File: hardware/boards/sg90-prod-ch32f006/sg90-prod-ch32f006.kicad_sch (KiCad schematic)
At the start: 21 parts, among them J1 Servo Input, J2 Debug, J3 Motor, J4 Potentiometer, Q1 BRCS150P02ZJ, U1 CH32V006F8U6, U2 DRV8837C, U3 74LVC1G07

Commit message: re-organize shared folders
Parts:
- removed C7: 10µF, Capacitor_SMD:C_0603_1608Metric, symbol Device:C
- added D1: PESD5V0L1UL, Diode_SMD:D_SOD-882, symbol Diode:PESD5V0L1UL
- added NT1, NT2, NT3, NT4: NetTie_2, shared:NetTie-2_SMD_0.2mm, symbol Device:NetTie_2
- J1: footprint common:Servo_Output_Pads -> shared:Servo_Output_Pads
- J2: footprint common:Debug_Pads_1x4_P1.27mm -> shared:Debug_Pads_1x4_P1.27mm
- J3: footprint common:Motor_Wire_Pads -> shared:Motor_Wire_Pads
- J4: footprint common:Pot_Wire_Pads -> shared:Pot_Wire_Pads
- Q1: footprint footprints:DFN-6L_L2.0-W2.0-P0.65-BL_BRCS300PXX -> shared:DFN-6L_L2.0-W2.0-P0.65-BL_BRCS300PXX; symbol common:BRCS150P02ZJ -> shared:BRCS150P02ZJ
- U1: renamed from U3; footprint footprints:TDFN-6_L1.0-W1.0-P0.35-BL -> shared:TDFN-6_L1.0-W1.0-P0.35-BL; symbol common:SN74LVC1G07DSFR_C42445855 -> shared:SN74LVC1G07DSFR_C42445855
- U3: renamed from U1; footprint common:UQFN-20_L3.0-W3.0-P0.40-BL-EP1.7 -> shared:UQFN-20_L3.0-W3.0-P0.40-BL-EP1.7; symbol common:CH32V006F8U6 -> shared:CH32V006F8U6
- renumbered C6 to C1, C1 to C2, C4 to C3, C3 to C4, C2 to C6, R4 to R1, R9 to R2, R2 to R4, R1 to R7
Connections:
- net V_MCU is gone; now on net +5V: J4.3 (Pin_3)
- net DATA: now also D1.1 (K), NT1.1; no longer U3.8 (PC1)
- net GND: now also R4.1, D1.2 (A); no longer R4.2
- net GND_MOT: now also R4.2, NT2.2; no longer R4.1, U3.2 (PA1/OPN0), U3.3 (PA2/OPP0)
- net MOT_A: now also J3.1 (Pin_1), NT3.2; no longer J3.2 (Pin_2), U3.16 (PD2)
- net MOT_B: now also J3.2 (Pin_2), NT4.2; no longer J3.1 (Pin_1), U3.17 (PD3)
- new net SEN_A: NT3.1, U3.16 (PD2/T1/T2/U2TX_/A3)
- new net SEN_B: NT4.1, U3.17 (PD3/T1/T2/U2RX_/NSS_/OPP2/A4)
- new net SEN_I: NT2.1, U3.2 (PA1/T1/T2/OPN0/XI/A1), U3.3 (PA2/T1/T2/U2TX_/OPP0/XO/A0)
- new net UART_RX: NT1.2, U3.8 (PC1/T1C2N_/T2/RX_/SDA/NSS)
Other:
- note added: "KELVIN TRACES"
- note added: "POTENTIOMETER"
- moved on the sheet: C3, C4, C5, C6, J1, R3, R4, R5, R7, U2, U3

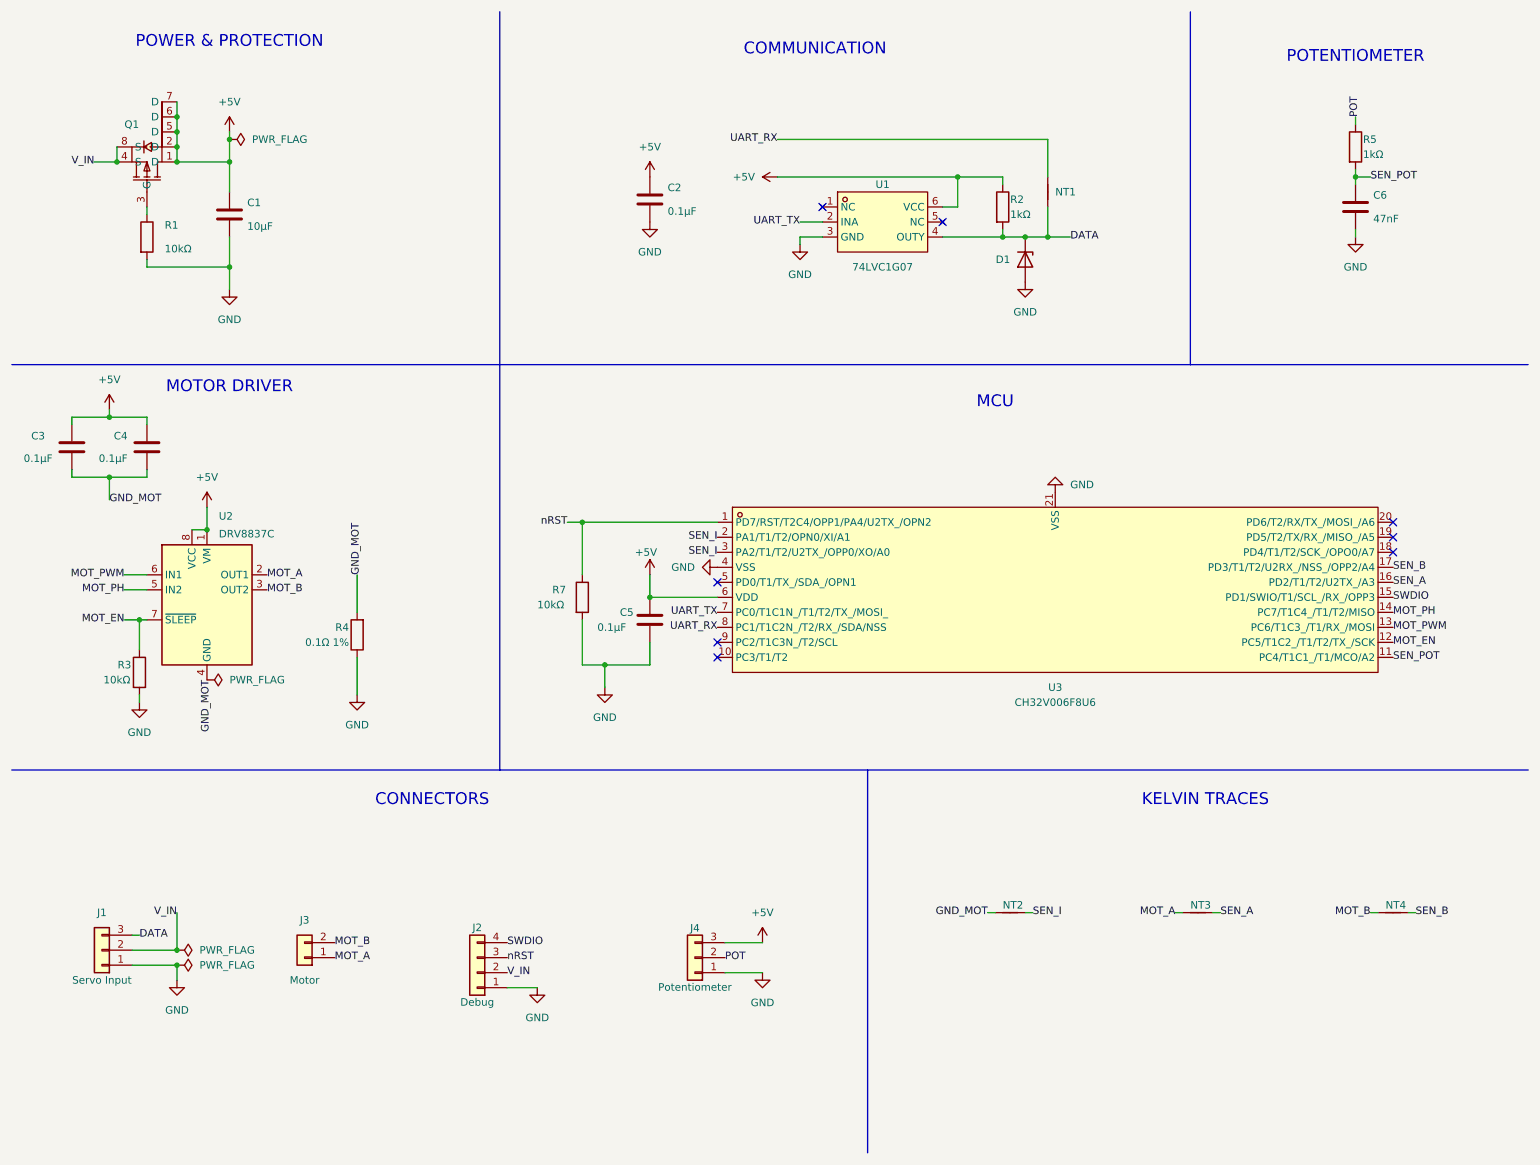
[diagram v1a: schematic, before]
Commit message: completed initial pass n sg90-prod-ch32f006
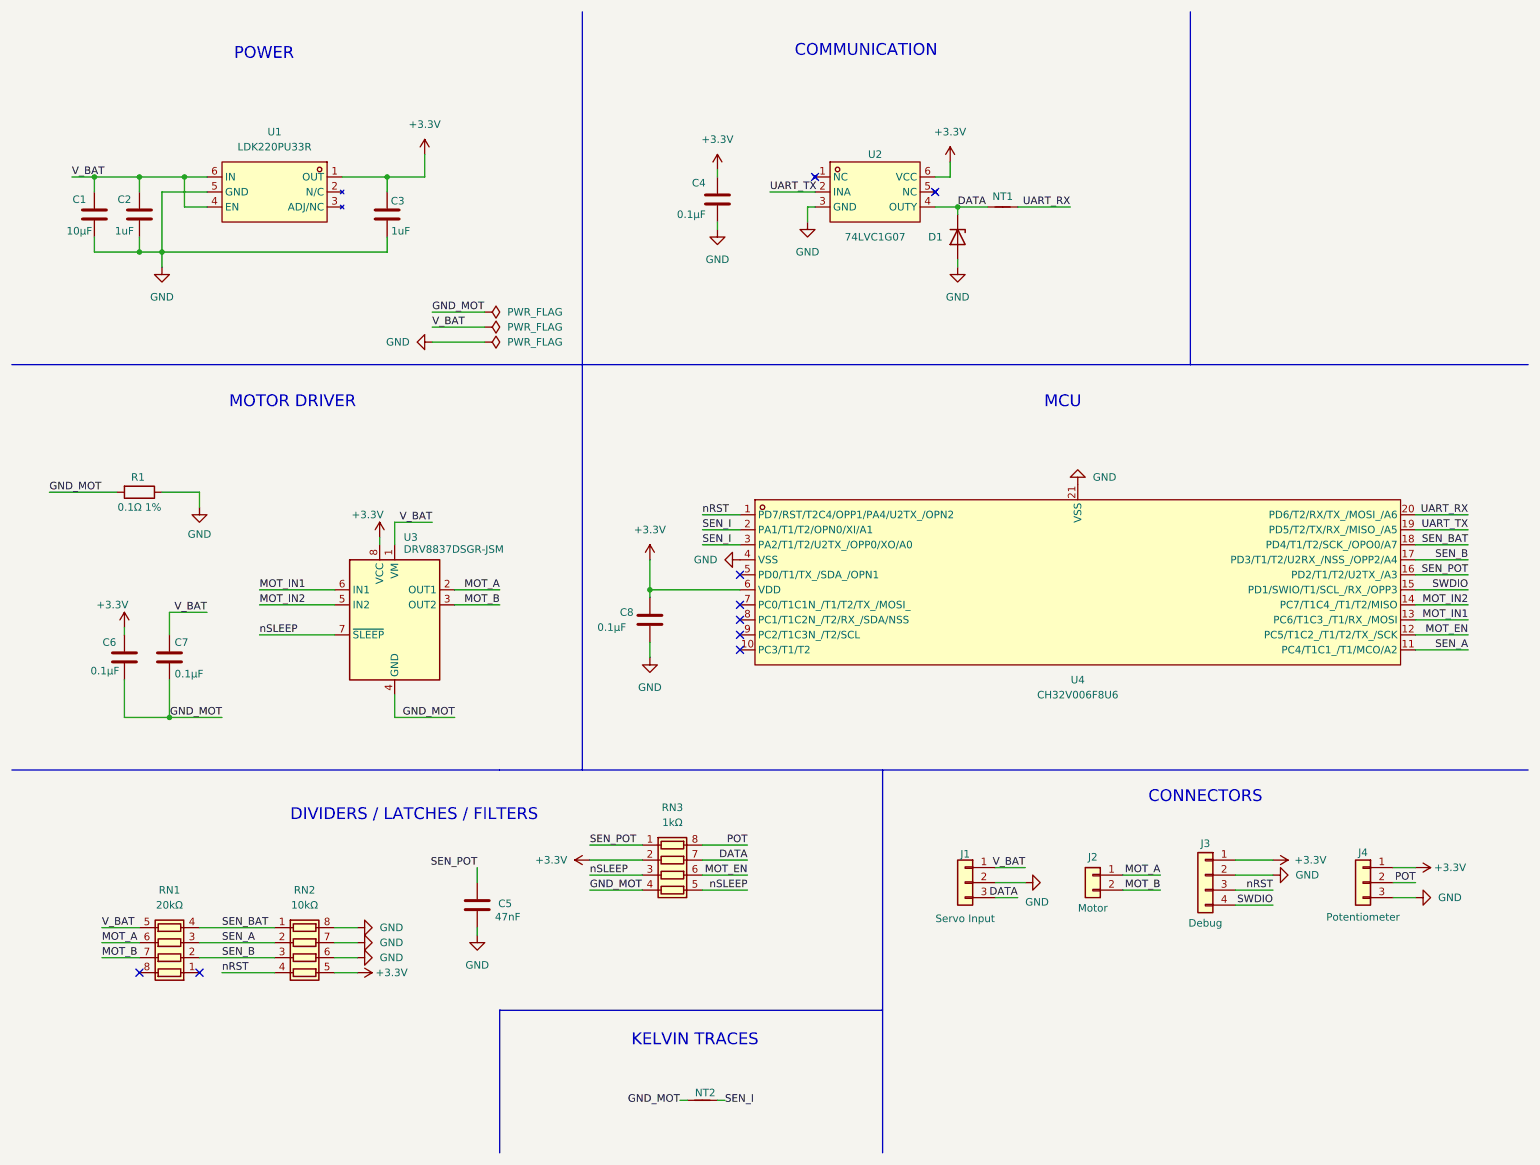
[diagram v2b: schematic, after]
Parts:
- removed NT3, NT4: NetTie_2, shared:NetTie-2_SMD_0.2mm, symbol Device:NetTie_2
- removed Q1: BRCS150P02ZJ, shared:DFN-6L_L2.0-W2.0-P0.65-BL_BRCS300PXX, symbol shared:BRCS150P02ZJ
- removed R1, R3, R7: 10kΩ, Resistor_SMD:R_0402_1005Metric, symbol Device:R
- removed R2, R5: 1kΩ, Resistor_SMD:R_0402_1005Metric, symbol Device:R
- added C2, C3: 1uF, Capacitor_SMD:C_0402_1005Metric, symbol Device:C
- added RN1: 20kΩ, Resistor_SMD:R_Array_Convex_4x0402, symbol Device:R_Pack04
- added RN2: 10kΩ, Resistor_SMD:R_Array_Convex_4x0402, symbol Device:R_Pack04
- added RN3: 1kΩ, Resistor_SMD:R_Array_Convex_4x0402, symbol Device:R_Pack04
- added U1: LDK220PU33R, shared:DFN-6_L1.3-W1.2-P0.40-BL, symbol shared:LDK220PU33R
- U3: renamed from U2; value DRV8837C -> DRV8837DSGR-JSM; LCSC (none) -> C22447132
- renumbered C2 to C4, C6 to C5, C3 to C6, C4 to C7, C5 to C8, J3 to J2, J2 to J3, R4 to R1, U1 to U2, U3 to U4
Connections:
- net V_IN is gone; now on net GND: J1.2 (Pin_2), J3.2 (Pin_2)
- net DATA: now also NT1.2, RN3.7 (R2.2); no longer NT1.1
- net GND: now also J4.3 (Pin_3), C2.2, C3.2, RN2.6 (R3.2), RN2.7 (R2.2), RN2.8 (R1.2), U1.5 (GND); no longer J1.1 (Pin_1), J3.1 (Pin_1), J4.1 (Pin_1)
- net GND_MOT: now also RN3.4 (R4.1)
- net MOT_A: now also RN1.6 (R3.2)
- net MOT_B: now also RN1.7 (R2.2)
- net MOT_EN: now also RN3.6 (R3.2); no longer U3.7 (~{SLEEP})
- net POT: now also RN3.8 (R1.2)
- net SEN_A: now also U4.11 (PC4/T1C1_/T1/MCO/A2), RN1.3 (R3.1), RN2.2 (R2.1); no longer U4.16 (PD2/T1/T2/U2TX_/A3)
- net SEN_B: now also RN1.2 (R2.1), RN2.3 (R3.1)
- net SEN_POT: now also U4.16 (PD2/T1/T2/U2TX_/A3), RN3.1 (R1.1); no longer U4.11 (PC4/T1C1_/T1/MCO/A2)
- net UART_RX: now also NT1.1, U4.20 (PD6/T2/RX/TX_/MOSI_/A6); no longer NT1.2, U4.8 (PC1/T1C2N_/T2/RX_/SDA/NSS)
- net UART_TX: now also U4.19 (PD5/T2/TX/RX_/MISO_/A5); no longer U4.7 (PC0/T1C1N_/T1/T2/TX_/MOSI_)
- net nRST: now also RN2.4 (R4.1)
- net SEN_BAT: now reaches U4.18 (PD4/T1/T2/SCK_/OPO0/A7)
- net SEN_BAT: now also RN1.4 (R4.1), RN2.1 (R1.1)
- net +5V renamed +3.3V
- net +3.3V: now also J3.1 (Pin_1), J4.1 (Pin_1), C3.1, RN2.5 (R4.2), RN3.2 (R2.1), U1.1 (OUT); no longer C1.1, C7.1, J4.3 (Pin_3), U3.1 (VM)
- net MOT_PH renamed MOT_IN2
- net MOT_PWM renamed MOT_IN1
- new net V_BAT: C1.1, C2.1, C7.1, J1.1 (Pin_1), RN1.5 (R4.2), U1.4 (EN), U1.6 (IN), U3.1 (VM)
- new net nSLEEP: RN3.3 (R3.1), RN3.5 (R4.2), U3.7 (~{SLEEP})
- no-connect marks 8 -> 9
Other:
- note added: "DIVIDERS / LATCHES / FILTERS"
- note added: "POWER"
- note removed: "POTENTIOMETER"
- note removed: "POWER & PROTECTION"
- moved on the sheet: C4, C5, C6, C7, D1, J1, J2, J3, J4, NT1, NT2, R1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

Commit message: finished first pass design of sg90-prod-ch32f006. It is ready for production
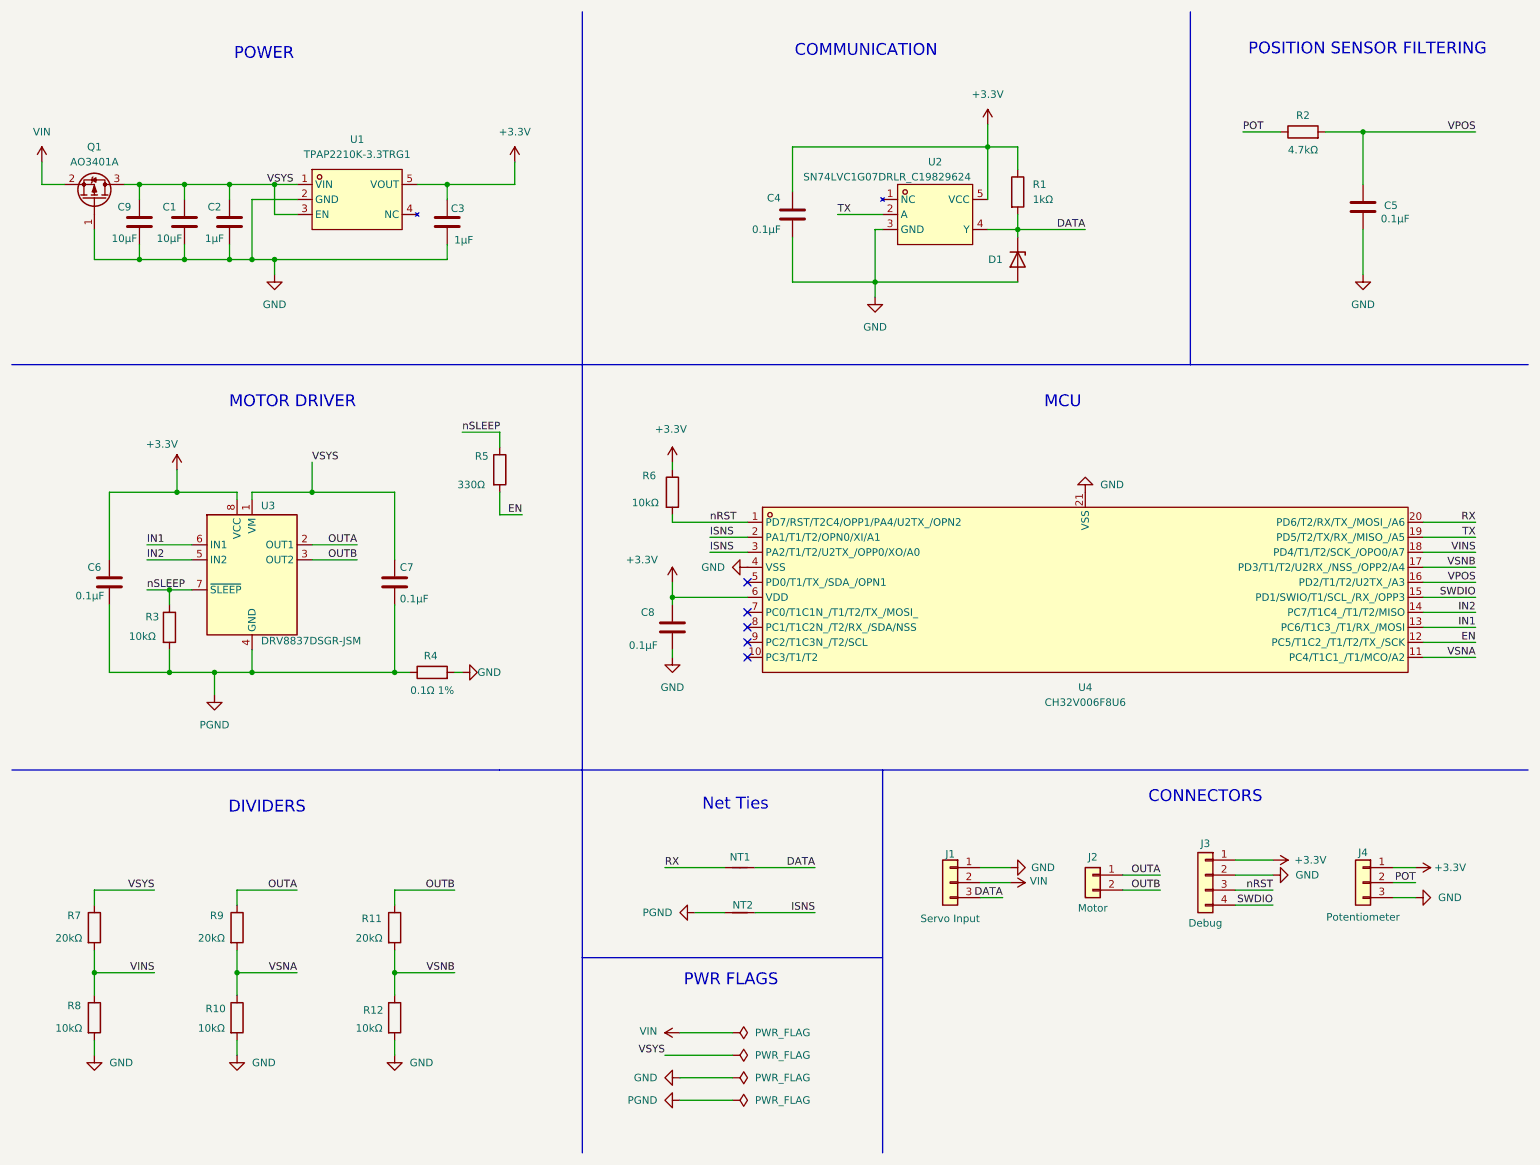
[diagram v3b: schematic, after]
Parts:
- removed RN1: 20kΩ, Resistor_SMD:R_Array_Convex_4x0402, symbol Device:R_Pack04
- removed RN2: 10kΩ, Resistor_SMD:R_Array_Convex_4x0402, symbol Device:R_Pack04
- removed RN3: 1kΩ, Resistor_SMD:R_Array_Convex_4x0402, symbol Device:R_Pack04
- removed U1: LDK220PU33R, shared:DFN-6_L1.3-W1.2-P0.40-BL, symbol shared:LDK220PU33R
- removed U2: 74LVC1G07, shared:TDFN-6_L1.0-W1.0-P0.35-BL, symbol shared:SN74LVC1G07DSFR_C42445855
- added C9: 10µF, Capacitor_SMD:C_0603_1608Metric, symbol Device:C
- added Q1: AO3401A, Package_TO_SOT_SMD:SOT-23, symbol Transistor_FET:AO3401A
- added R1: 1kΩ, Resistor_SMD:R_0402_1005Metric, symbol Device:R
- added R10, R12, R3, R6, R8: 10kΩ, Resistor_SMD:R_0402_1005Metric, symbol Device:R
- added R11, R7, R9: 20kΩ, Resistor_SMD:R_0402_1005Metric, symbol Device:R
- added R2: 4.7kΩ, Resistor_SMD:R_0402_1005Metric, symbol Device:R
- added R5: 330Ω, Resistor_SMD:R_0402_1005Metric, symbol Device:R
- added U1: TPAP2210K-3.3TRG1, shared:SOT-23-5_L2.9-W1.6-P0.95-LS2.8-BR, symbol shared:TPAP2210K-3.3TRG1
- added U2: SN74LVC1G07DRLR_C19829624, shared:SOT-553-5_L1.6-W1.2-P0.50-LS1.6-BL, symbol shared:SN74LVC1G07DRLR_C19829624
- C2, C3: value 1uF -> 1µF
- C5: value 47nF -> 0.1µF
- J1, J2, J3, J4: now left out of the parts list
- R4: renamed from R1; footprint Resistor_SMD:R_0603_1608Metric -> Resistor_SMD:R_1206_3216Metric
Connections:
- net +3.3V: now also R1.1, R6.1, U1.5 (VOUT), U2.5 (VCC)
- net DATA: now also R1.2, U2.4 (Y)
- net GND: now also J1.1 (Pin_1), R4.2, C9.2, Q1.1 (G), R10.2, R12.2, R8.2, U1.2 (GND), U2.3 (GND); no longer J1.2 (Pin_2), R4.1
- net POT: now also R2.1
- net nRST: now also R6.2
- net nSLEEP: now also R3.1, R5.1
- net GND_MOT renamed PGND
- net PGND: now also R4.1, R3.2; no longer R4.2
- net MOT_A renamed OUTA
- net OUTA: now also R9.1
- net MOT_B renamed OUTB
- net OUTB: now also R11.1
- net MOT_EN renamed EN
- net EN: now also R5.2
- net MOT_IN1 renamed IN1
- net MOT_IN2 renamed IN2
- net SEN_A renamed VSNA
- net VSNA: now also R10.1, R9.2
- net SEN_B renamed VSNB
- net VSNB: now also R11.2, R12.1
- net SEN_BAT renamed VINS
- net VINS: now also R7.2, R8.1
- net SEN_I renamed ISNS
- net SEN_POT renamed VPOS
- net VPOS: now also R2.2
- net UART_RX renamed RX
- net UART_TX renamed TX
- net TX: now also U2.2 (A)
- net V_BAT renamed VSYS
- net VSYS: now also C9.1, Q1.3 (D), R7.1, U1.1 (VIN), U1.3 (EN); no longer J1.1 (Pin_1)
- new net VIN: J1.2 (Pin_2), Q1.2 (S)
- no-connect marks 9 -> 5
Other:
- note added: "DIVIDERS"
- note added: "Net Ties"
- note added: "POSITION SENSOR FILTERING"
- note added: "PWR FLAGS"
- note removed: "DIVIDERS / LATCHES / FILTERS"
- note removed: "KELVIN TRACES"
- moved on the sheet: C1, C2, C3, C4, C5, C6, C7, C8, D1, J1, NT1, NT2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
